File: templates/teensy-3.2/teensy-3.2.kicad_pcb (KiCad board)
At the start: 2 copper layers, 1 part, among them J1 TEENSY LC

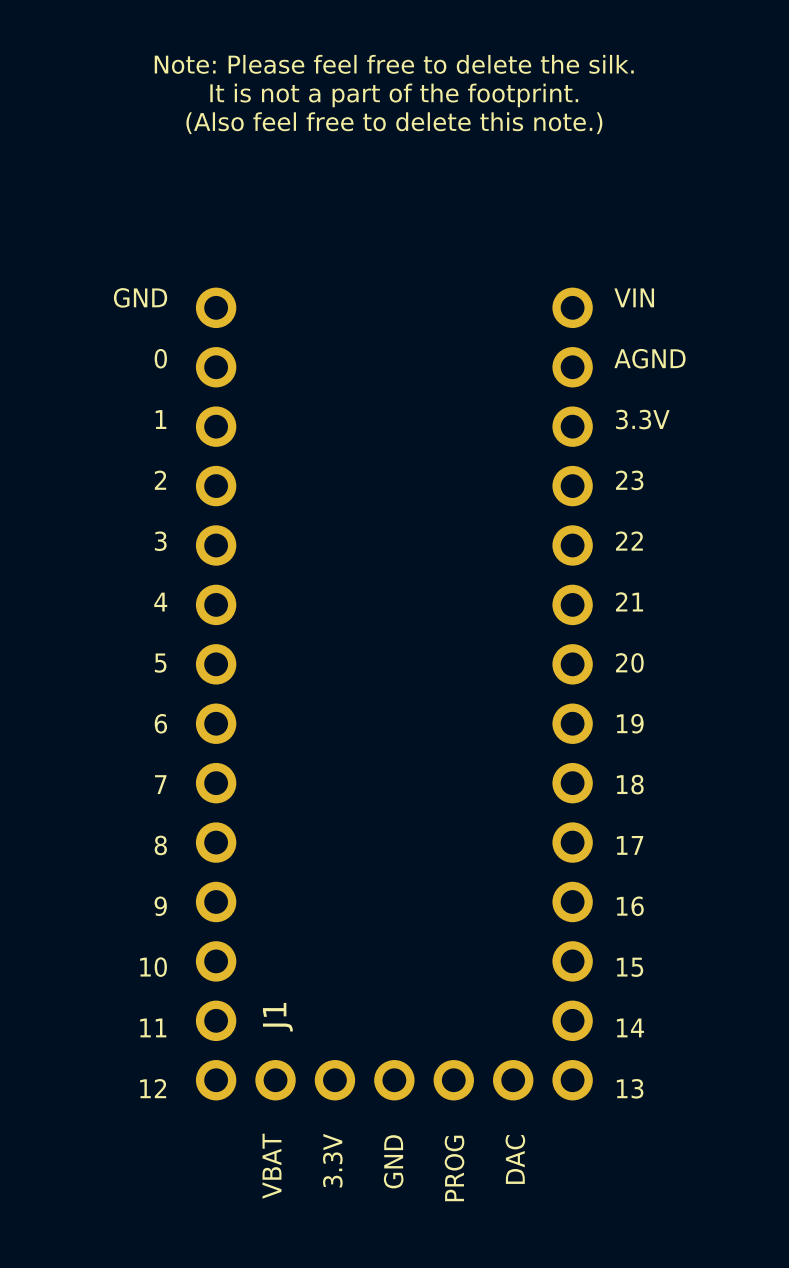
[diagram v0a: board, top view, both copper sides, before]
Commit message: Moved wickerbox templates out. Teensy is messed up.
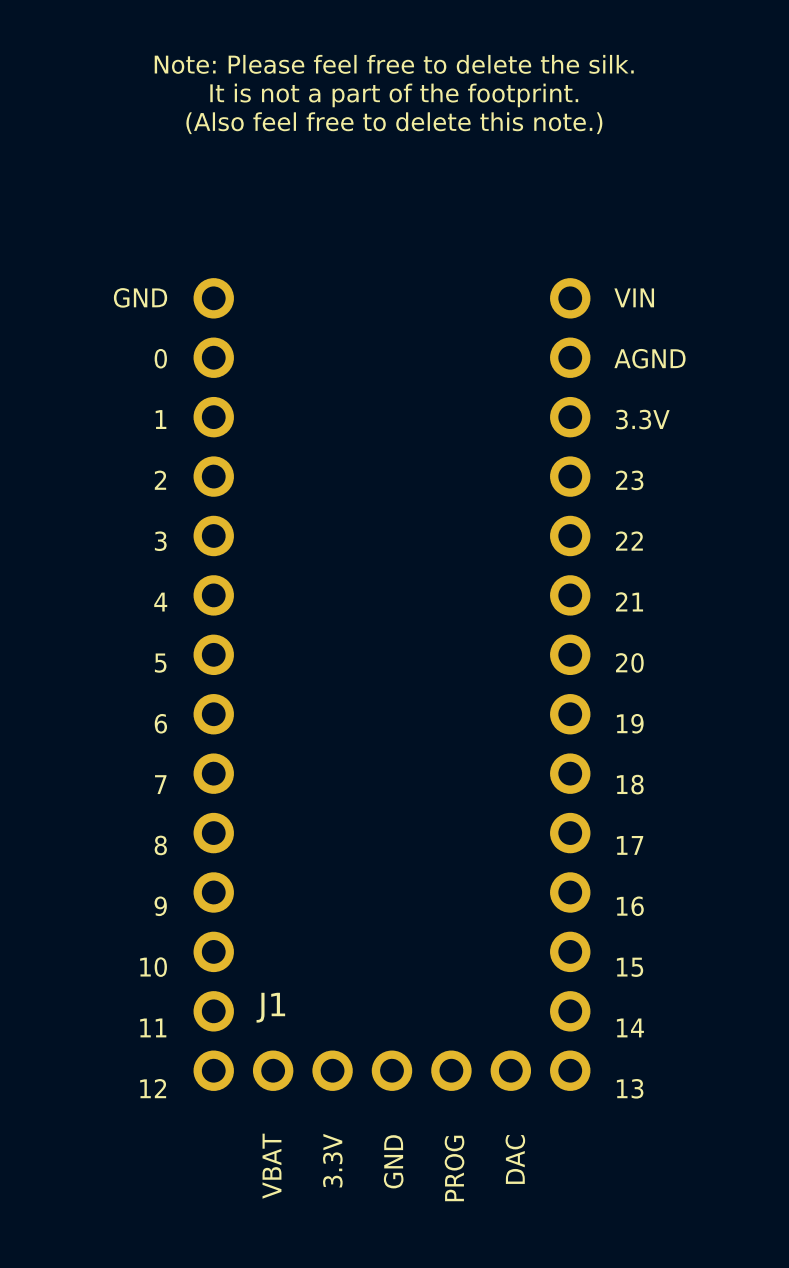
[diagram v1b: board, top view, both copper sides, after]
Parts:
- J1: value TEENSY LC -> TEENSY3.2-72MHz; footprint TEENSY-LC -> Wickerlib:TEENSY-3.2-NOSILK
- moved J1 6.00 mm to (102.4, 88.0)
